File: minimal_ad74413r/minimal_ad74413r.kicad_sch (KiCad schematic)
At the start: 60 parts, among them J1 FW-02-03-G-D-085-155, J2 FW-02-03-G-D-085-155, J3 FW-02-03-G-D-085-155, J4 FW-02-03-G-D-085-155, J5 FW-02-03-G-D-085-155, J6 FW-02-03-G-D-085-155, J7 FW-14-03-G-D-085-155, U1 AD74413RBCPZ

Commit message: Development backup
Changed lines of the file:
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@@
 		(fields_autoplaced yes)
 		(property "Reference" "J4"
-			(at 171.45 30.4799 90)
+			(at 161.29 30.4799 90)
 			(effects
 				(font
 					(size 1.27 1.27)
 				)
-				(justify left)
+				(justify right)
 			)
 		)
 		(property "Value" "FW-02-03-G-D-085-155"
-			(at 171.45 33.0199 90)
+			(at 161.29 33.0199 90)
 			(effects
 				(font
 					(size 1.27 1.27)
 				)
-				(justify left)
+				(justify right)
 			)
 		)

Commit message: Development backup
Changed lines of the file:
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@@
 		(dnp no)
 		(fields_autoplaced yes)
-		(property "Reference" "#PWR7"
+		(property "Reference" "#PWR11"
 			(at 233.68 68.58 0)
 			(effects
@@
 			(project "minimal_ad74413r"
 				(path "/3d1a8eae-9f4e-4ae3-8a80-a6e3408e9f8d"
-					(reference "#PWR7")
+					(reference "#PWR11")
 					(unit 1)
 				)
@@
 		(dnp no)
 		(fields_autoplaced yes)
-		(property "Reference" "#PWR22"
+		(property "Reference" "#PWR3"
 			(at 162.56 74.93 0)
 			(effects
@@
 			(project "minimal_ad74413r"
 				(path "/3d1a8eae-9f4e-4ae3-8a80-a6e3408e9f8d"
-					(reference "#PWR22")
+					(reference "#PWR3")
 					(unit 1)
 				)
@@
 		(dnp no)
 		(fields_autoplaced yes)
-		(property "Reference" "#PWR29"
+		(property "Reference" "#PWR2"
 			(at 137.16 187.96 0)
 			(effects
@@
 			(project "minimal_ad74413r"
 				(path "/3d1a8eae-9f4e-4ae3-8a80-a6e3408e9f8d"
-					(reference "#PWR29")
+					(reference "#PWR2")
 					(unit 1)
 				)
@@
 		(dnp no)
 		(fields_autoplaced yes)
-		(property "Reference" "#PWR6"
+		(property "Reference" "#PWR10"
 			(at 228.6 52.07 0)
 			(effects
@@
 			(project "minimal_ad74413r"
 				(path "/3d1a8eae-9f4e-4ae3-8a80-a6e3408e9f8d"
-					(reference "#PWR6")
+					(reference "#PWR10")
 					(unit 1)
 				)
@@
 		(dnp no)
 		(fields_autoplaced yes)
-		(property "Reference" "#PWR32"
+		(property "Reference" "#PWR15"
 			(at 284.48 137.16 0)
 			(effects
@@
 			(project "minimal_ad74413r"
 				(path "/3d1a8eae-9f4e-4ae3-8a80-a6e3408e9f8d"
-					(reference "#PWR32")
+					(reference "#PWR15")
 					(unit 1)
 				)
@@
 		(dnp no)
 		(fields_autoplaced yes)
-		(property "Reference" "#PWR9"
+		(property "Reference" "#PWR14"
 			(at 243.84 104.14 0)
 			(effects
@@
 			(project "minimal_ad74413r"
 				(path "/3d1a8eae-9f4e-4ae3-8a80-a6e3408e9f8d"
-					(reference "#PWR9")
+					(reference "#PWR14")
 					(unit 1)
 				)
@@
 		(dnp no)
 		(fields_autoplaced yes)
-		(property "Reference" "#PWR36"
+		(property "Reference" "#PWR18"
 			(at 284.48 220.98 0)
 			(effects
@@
 			(project "minimal_ad74413r"
 				(path "/3d1a8eae-9f4e-4ae3-8a80-a6e3408e9f8d"
-					(reference "#PWR36")
+					(reference "#PWR18")
 					(unit 1)
 				)
@@
 		(dnp no)
 		(fields_autoplaced yes)
-		(property "Reference" "#PWR33"
+		(property "Reference" "#PWR16"
 			(at 284.48 165.1 0)
 			(effects
@@
 			(project "minimal_ad74413r"
 				(path "/3d1a8eae-9f4e-4ae3-8a80-a6e3408e9f8d"
-					(reference "#PWR33")
+					(reference "#PWR16")
 					(unit 1)
 				)
@@
 		(dnp no)
 		(fields_autoplaced yes)
-		(property "Reference" "#PWR30"
+		(property "Reference" "#PWR1"
 			(at 121.92 187.96 0)
 			(effects
@@
 			(project "minimal_ad74413r"
 				(path "/3d1a8eae-9f4e-4ae3-8a80-a6e3408e9f8d"
-					(reference "#PWR30")
+					(reference "#PWR1")
 					(unit 1)
 				)
@@
 		(dnp no)
 		(fields_autoplaced yes)
-		(property "Reference" "#PWR4"
+		(property "Reference" "#PWR8"
 			(at 175.26 52.07 0)
 			(effects
@@
 			(project "minimal_ad74413r"
 				(path "/3d1a8eae-9f4e-4ae3-8a80-a6e3408e9f8d"
-					(reference "#PWR4")
+					(reference "#PWR8")
 					(unit 1)
 				)
@@
 		(dnp no)
 		(fields_autoplaced yes)
-		(property "Reference" "#PWR2"
+		(property "Reference" "#PWR7"
 			(at 170.18 219.71 0)
 			(effects
@@
 			(project "minimal_ad74413r"
 				(path "/3d1a8eae-9f4e-4ae3-8a80-a6e3408e9f8d"
-					(reference "#PWR2")
+					(reference "#PWR7")
 					(unit 1)
 				)
@@
 		(dnp no)
 		(fields_autoplaced yes)
-		(property "Reference" "#PWR3"
+		(property "Reference" "#PWR6"
 			(at 167.64 109.22 0)
 			(effects
@@
 			(project "minimal_ad74413r"
 				(path "/3d1a8eae-9f4e-4ae3-8a80-a6e3408e9f8d"
-					(reference "#PWR3")
+					(reference "#PWR6")
 					(unit 1)
 				)
@@
 		(dnp no)
 		(fields_autoplaced yes)
-		(property "Reference" "#PWR8"
+		(property "Reference" "#PWR12"
 			(at 238.76 86.36 0)
 			(effects
@@
 			(project "minimal_ad74413r"
 				(path "/3d1a8eae-9f4e-4ae3-8a80-a6e3408e9f8d"
-					(reference "#PWR8")
+					(reference "#PWR12")
 					(unit 1)
 				)
@@
 		(dnp no)
 		(fields_autoplaced yes)
-		(property "Reference" "#PWR1"
+		(property "Reference" "#PWR4"
 			(at 162.56 87.63 0)
 			(effects
@@
 			(project "minimal_ad74413r"
 				(path "/3d1a8eae-9f4e-4ae3-8a80-a6e3408e9f8d"
-					(reference "#PWR1")
+					(reference "#PWR4")
 					(unit 1)
 				)
@@
 		(on_board yes)
 		(dnp no)
-		(property "Reference" "#PWR28"
+		(property "Reference" "#PWR5"
 			(at 167.64 45.72 0)
 			(effects
@@
 			(project "minimal_ad74413r"
 				(path "/3d1a8eae-9f4e-4ae3-8a80-a6e3408e9f8d"
-					(reference "#PWR28")
+					(reference "#PWR5")
 					(unit 1)
 				)
@@
 		(dnp no)
 		(fields_autoplaced yes)
-		(property "Reference" "#PWR5"
+		(property "Reference" "#PWR9"
 			(at 203.2 243.84 0)
 			(effects
@@
 			(project "minimal_ad74413r"
 				(path "/3d1a8eae-9f4e-4ae3-8a80-a6e3408e9f8d"
-					(reference "#PWR5")
+					(reference "#PWR9")
 					(unit 1)
 				)
@@
 		(dnp no)
 		(fields_autoplaced yes)
-		(property "Reference" "#PWR34"
+		(property "Reference" "#PWR17"
 			(at 284.48 193.04 0)
 			(effects
@@
 			(project "minimal_ad74413r"
 				(path "/3d1a8eae-9f4e-4ae3-8a80-a6e3408e9f8d"
-					(reference "#PWR34")
+					(reference "#PWR17")
 					(unit 1)
 				)
@@
 		(on_board yes)
 		(dnp no)
-		(property "Reference" "#PWR27"
+		(property "Reference" "#PWR13"
 			(at 241.3 45.72 0)
 			(effects
@@
 			(project "minimal_ad74413r"
 				(path "/3d1a8eae-9f4e-4ae3-8a80-a6e3408e9f8d"
-					(reference "#PWR27")
+					(reference "#PWR13")
 					(unit 1)
 				)

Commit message: Development backup
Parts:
- removed J3, J4: FW-02-03-G-D-085-155, connector_footprints:FW-02-03-G-D-085-155, symbol UNITED_CONNECTORS_DATA_BASE:J_FW-02-03-G-D-085-155
- removed MB3, MB4: mouse-bite-midle-50mil-200mil, mouse_bite_footprints:mouse-bite-midle-50mil-200mil, symbol UNITED_MOUSE_BITES_DATA_BASE:mouse-bite-midle-50mil-200mil
- removed TP25, TP26: TestPoint, test_point_footprints:TestPoint_THTPad_Castelated, symbol UNITED_TEST_POINTS:TestPoint_Castelated
- added C33: 4.7 µF, capacitor_footprints:C_1210_200_3225Metric, symbol UNITED_CAPACITORS_DATA_BASE:C_GCM32DC72A475KE02K
- added C34, C35, C36, C41, C43: 100 nF, capacitor_footprints:C_0402_1005Metric, symbol UNITED_CAPACITORS_DATA_BASE:C_GCM155R71H104KE02D
- added C37, C38: 10 µF, capacitor_footprints:C_1206_3216Metric, symbol UNITED_CAPACITORS_DATA_BASE:C_CL31B106KBHNNN#
- added C39: 4.7 µF, capacitor_footprints:C_0603_1608Metric, symbol UNITED_CAPACITORS_DATA_BASE:C_C1608X7S1A475K080AC
- added C40, C42: 1 nF, capacitor_footprints:C_0402_1005Metric, symbol UNITED_CAPACITORS_DATA_BASE:C_GCM155R71H102KA37D
- added D5: 62.0 V, diode_footprints:SOD_123, symbol UNITED_DIODES_DATA_BASE:D_MMSZ5265BT1G
- added D6: 100.0 V, diode_footprints:PowerDI_123, symbol UNITED_DIODES_DATA_BASE:D_DFLS1200-7
- added D7: 200.0 V, diode_footprints:SOD_123F, symbol UNITED_DIODES_DATA_BASE:D_US1DWF
- added J8: FW-02-03-G-D-085-155, connector_footprints:FW-02-03-G-D-085-155, symbol UNITED_CONNECTORS_DATA_BASE:J_FW-02-03-G-D-085-155
- added JP1: SolderJumper_3_Open, solder_jumper_footprints:SolderJumper-3_P1.3mm_Open_RoundedPad1.0x1.5mm_NumberLabels, symbol UNITED_SOLDER_JUMPERS:SolderJumper_3_Open
- added JP2, JP3: SolderJumper_2_Bridged, solder_jumper_footprints:SolderJumper-2_P1.3mm_Bridged_RoundedPad1.0x1.5mm, symbol UNITED_SOLDER_JUMPERS:SolderJumper_2_Bridged
- added L1: 100 µH, inductor_footprints:XFL3012, symbol UNITED_INDUCTORS_DATA_BASE:L_XFL3012-104ME
- added R21, R22, R23, R24, R25, R26, R27, R28: 100 kΩ, resistor_footprints:R_0402_1005Metric, symbol UNITED_RESISTORS_DATA_BASE:R_ERJ-2GEJ104X
- added T1: ZA9644-AED, transformer_footprints:ZA9644, symbol UNITED_TRANSFORMERS_DATA_BASE:T_ZA9644-AED
- added U2: ADP1032ACPZ-5-R7, analog_devices_footprints:CP-41-1_ADI, symbol UNITED_IC_ADI:U_ADP1032ACPZ-5-R7
- added U3: MAX22440CAEE+, analog_devices_footprints:21-0055_E16MS&plus_1F_ADI, symbol UNITED_IC_ADI:U_MAX22440CAEE+
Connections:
- net 3V3: now also C35.1, C36.1, C42.1, C43.1, JP2.2, R23.1, R25.1, R27.1, U2.10 (SVDD1), U2.20 (SVDD2), U3.1 (VDDA); no longer J7.13, TP19.1
- net GNDA: now also C35.2, C36.2, C37.2, C38.2, C39.2, C42.2, C43.2, R22.1, R24.2, R26.2, R28.2, T1.8, U2.16 (SGND2), U2.27 (SGND2), U2.4 (SGND2), U2.44 (EPGND2), U2.5 (SGND1), U3.2 (GNDA), U3.8 (GNDA); no longer J7.10, J7.11, J7.12, J7.14, J7.16, J7.18, J7.2, J7.20, J7.22, J7.24, J7.26, J7.28, J7.4, J7.6, J7.8, TP18.1, TP5.1, TP6.1
- net GPO_A: now also J7.23, TP8.1, U3.14 (OUT1); no longer J7.27, U1.19 (GPO_A)
- net GPO_B: now also J7.21, TP7.1, U3.13 (OUT2); no longer J7.25, U1.20 (GPO_B)
- net GPO_C: now also J7.19, TP14.1, U3.12 (OUT3); no longer J7.1, TP13.1, U1.21 (GPO_C)
- net GPO_D: now also J7.17, TP13.1, U3.11 (OUT4); no longer J7.3, TP14.1, U1.22 (GPO_D)
- net SCLK: now also R23.2, U2.9 (SCK); no longer J7.17, TP21.1
- net SDI: now also R28.1, U2.8 (SI); no longer J7.19, TP22.1
- net SDO: now also R24.1, U2.7 (SO); no longer J7.5, TP15.1
- net VDD_24V: now also JP3.2; no longer TP7.1, TP8.1
- net ~{ADC_RDY}: now also J7.15, TP17.1; no longer J7.7, TP16.1
- net ~{ALERT}: now also R27.2, U2.21 (SGPI3); no longer J7.9, TP17.1
- net ~{LDAC}: now also R26.1, U2.22 (SGPO2); no longer J7.15, TP20.1
- net ~{RESET}: now also R25.2, U2.23 (SGPO1); no longer J7.23, TP24.1
- net ~{SYNC}: now also U2.6 (~{SSS}); no longer J7.21, TP23.1
- new net: D5.1, D6.1
- new net: R22.2, U2.14 (SYNC)
- new net: R21.2, U2.35 (PWRGD)
- new net: D7.2, T1.5
- new net GND: C33.1, J8.1, J8.2, JP1.3 (B), TP16.1, U2.28 (PGNDP), U2.33 (GNDP), U2.43 (EPGNDP)
- new net GNDD: C34.2, C40.2, C41.2, J7.10, J7.12, J7.14, J7.16, J7.18, J7.2, J7.20, J7.22, J7.24, J7.25, J7.26, J7.4, J7.6, J7.8, TP6.1, U2.3 (MGND), U2.34 (MGND), U2.42 (EPGNDM), U3.15 (GNDB), U3.9 (GNDB)
- new net GPO_A_ISO: U1.19 (GPO_A), U3.3 (IN1)
- new net GPO_B_ISO: U1.20 (GPO_B), U3.4 (IN2)
- new net GPO_C_ISO: U1.21 (GPO_C), U3.5 (IN3)
- new net GPO_D_ISO: U1.22 (GPO_D), U3.6 (IN4)
- new net MCK: J7.7, TP21.1, U2.40 (MCK)
- new net MGPI1: J7.1, TP24.1, U2.36 (MGPI1)
- new net MGPI2: J7.3, TP23.1, U2.37 (MGPI2)
- new net MGPO3: J7.5, TP22.1, U2.38 (MGPO3)
- new net MI: J7.11, TP19.1, U2.1 (MI)
- new net MO: J7.9, TP20.1, U2.41 (MO)
- new net MVDD: C34.1, C40.1, C41.1, J7.27, J7.28, R21.1, TP5.1, U2.39 (MVDD), U3.10 (ENB), U3.16 (VDDB)
- new net SLEW: JP1.2 (C), U2.32 (SLEW)
- new net SW2: L1.1, U2.17 (SW2)
- new net SWP: D6.2, T1.4, U2.29 (SWP)
- new net VINP: C33.2, D5.2, J8.3, J8.4, JP1.1 (A), T1.1, TP15.1, U2.30 (VINP), U2.31 (EN)
- new net VOUT1: C37.1, C38.1, D7.1, JP3.1, U2.18 (VOUT1)
- new net VOUT2: C39.1, JP2.1, L1.2, U2.15 (VOUT2)
- new net ~{MSS}: J7.13, TP18.1, U2.2 (~{MSS})
- no-connect marks 1 -> 2
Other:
- moved on the sheet: C1, C14, C15, C16, C17, C18, C19, C2, C20, C29, C3, C30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

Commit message: Development backup
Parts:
- removed C40, C42: 1 nF, capacitor_footprints:C_0402_1005Metric, symbol UNITED_CAPACITORS_DATA_BASE:C_GCM155R71H102KA37D
- removed C41, C43: 100 nF, capacitor_footprints:C_0402_1005Metric, symbol UNITED_CAPACITORS_DATA_BASE:C_GCM155R71H104KE02D
- removed U3: MAX22440CAEE+, analog_devices_footprints:21-0055_E16MS&plus_1F_ADI, symbol UNITED_IC_ADI:U_MAX22440CAEE+
- added C44, C45: 100 nF, capacitor_footprints:C_0402_1005Metric, symbol UNITED_CAPACITORS_DATA_BASE:C_GCM155R71H104KE02D
- added J9: FW-02-03-G-D-085-155, connector_footprints:FW-02-03-G-D-085-155, symbol UNITED_CONNECTORS_DATA_BASE:J_FW-02-03-G-D-085-155
- added MB8, MB9: mouse-bite-midle-50mil-200mil, mouse_bite_footprints:mouse-bite-midle-50mil-200mil, symbol UNITED_MOUSE_BITES_DATA_BASE:mouse-bite-midle-50mil-200mil
- added TP25, TP26: TestPoint, test_point_footprints:TestPoint_THTPad_Castelated, symbol UNITED_TEST_POINTS:TestPoint_Castelated
- added U4: MAX22166EAEE+T, analog_devices_footprints:21-0055_E16MS&plus_2_MXM_ADI, symbol UNITED_IC_ADI:U_MAX22166EAEE+T
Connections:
- net 3V3: now also C44.1, U4.1 (VDDA)
- net GND: now also J8.3; no longer J8.2
- net GNDA: now also C44.2, J9.1, J9.3, TP26.1, U4.8 (GNDA)
- net GNDD: now also J7.17, J7.28, TP13.1, C45.2, U4.9 (GNDB); no longer J7.16, J7.25, TP6.1
- net GPO_A: now also J7.27, TP5.1, U4.14 (OUT2); no longer J7.23, TP8.1
- net GPO_A_ISO: now also U4.3 (IN2)
- net GPO_B: now also J7.25, TP6.1, U4.13 (OUT3); no longer J7.21, TP7.1
- net GPO_B_ISO: now also U4.4 (IN3)
- net GPO_C: now also J7.23, TP8.1, U4.12 (OUT4); no longer J7.19, TP14.1
- net GPO_C_ISO: now also U4.5 (IN4)
- net GPO_D: now also J7.21, TP7.1, U4.11 (OUT5); no longer J7.17, TP13.1
- net GPO_D_ISO: now also U4.6 (IN5)
- net MVDD: now also J7.15, J7.16, TP17.1, C45.1, U4.16 (VDDB); no longer J7.27, J7.28, TP5.1
- net VDD_24V: now also J9.2, J9.4, TP25.1
- net VINP: now also J8.2; no longer J8.3
- net ~{ADC_RDY}: now also J7.19, TP14.1, U4.10 (OUT6); no longer J7.15, TP17.1, U1.52 (~{ADC_RDY})
- new net ~{ADC_RDY_ISO}: U1.52 (~{ADC_RDY}), U4.7 (IN6)
- no-connect marks 2 -> 4
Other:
- moved on the sheet: J8, TP15, TP16

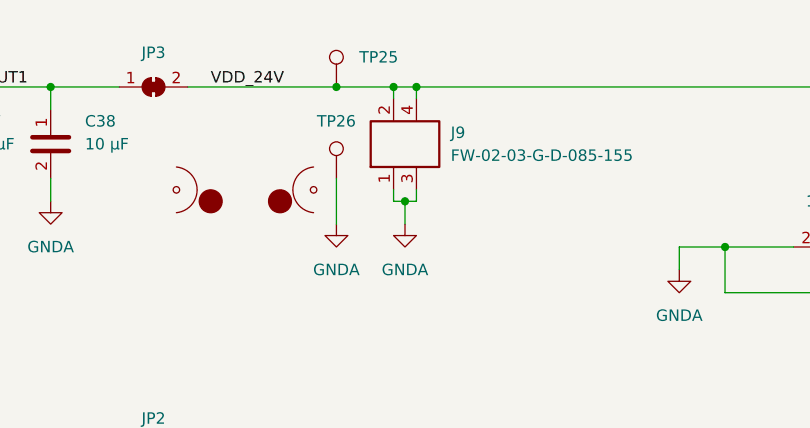
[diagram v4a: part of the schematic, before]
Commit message: update minimal_ad74413r footprint
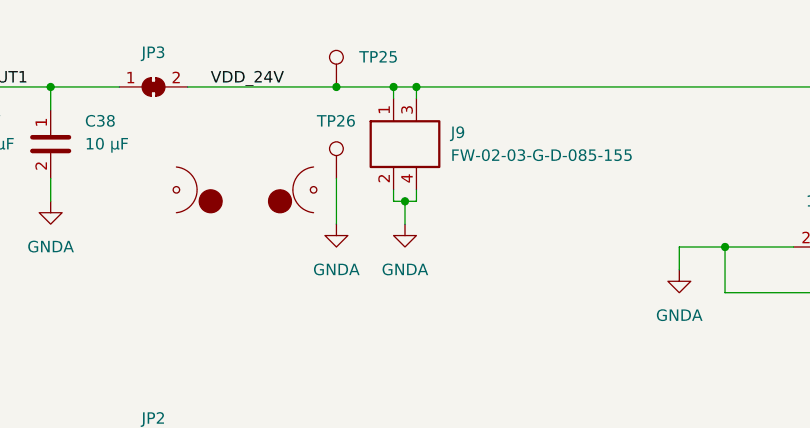
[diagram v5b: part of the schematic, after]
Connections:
- net GNDA: now also J9.2, J9.4; no longer J9.1, J9.3
- net VDD_24V: now also J9.1, J9.3; no longer J9.2, J9.4
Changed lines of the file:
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@@
 		(lib_id "UNITED_CONNECTORS_DATA_BASE:J_FW-02-03-G-D-085-155")
 		(at 215.9 34.29 90)
+		(mirror x)
 		(unit 1)
 		(exclude_from_sim no)
@@
 		)
 		(property "Footprint" "connector_footprints:FW-02-03-G-D-085-155"
-			(at 223.52 29.21 0)
+			(at 223.52 39.37 0)
 			(show_name yes)
 			(effects
@@
 		)
 		(property "Datasheet" "https://suddendocs.samtec.com/catalog_english/fw_sm.pdf?_gl=1*1xtxv9c*_gcl_au*MTM0MTYyNTQ5MS4xNzM2MDk5MTUz*_ga*MTYxNDYyMTQ0Mi4xNzM2MDk5MTUz*_ga_3KFNZC07WW*MTczODE2NTI0NS4zMi4xLjE3MzgxNjU1NjMuNjAuMC4w"
-			(at 226.06 29.21 0)
+			(at 226.06 39.37 0)
 			(show_name yes)
 			(effects
@@
 		)
 		(property "Description" "Samtec FW-xx-03-G-D-085-155 series,  2 positions connector,  1.27 mm pitch,  Black,  Vertical mounting,  5.2 A,  300 V,  Surface Mount,  Gold plated"
-			(at 228.6 29.21 0)
+			(at 228.6 39.37 0)
 			(show_name yes)
 			(effects
@@
 		)
 		(property "Color" "Black"
-			(at 231.14 29.21 0)
+			(at 231.14 39.37 0)
 			(show_name yes)
 			(effects
@@
 		)
 		(property "Contact Plating" "Gold"
-			(at 233.68 29.21 0)
+			(at 233.68 39.37 0)
 			(show_name yes)
 			(effects
@@
 		)
 		(property "Current Rating (A)" "5.2"
-			(at 236.22 29.21 0)
+			(at 236.22 39.37 0)
 			(show_name yes)
 			(effects
@@
 		)
 		(property "MPN" "FW-02-03-G-D-085-155"
-			(at 238.76 29.21 0)
+			(at 238.76 39.37 0)
 			(show_name yes)
 			(effects
@@
 		)
 		(property "Manufacturer" "Samtec"
-			(at 241.3 29.21 0)
+			(at 241.3 39.37 0)
 			(show_name yes)
 			(effects
@@
 		)
 		(property "Mounting Angle" "Vertical"
-			(at 243.84 29.21 0)
+			(at 243.84 39.37 0)
 			(show_name yes)
 			(effects
@@
 		)
 		(property "Mounting Style" "Surface Mount"
-			(at 246.38 29.21 0)
+			(at 246.38 39.37 0)
 			(show_name yes)
 			(effects
@@
 		)
 		(property "Number of Rows" "2"
-			(at 248.92 29.21 0)
+			(at 248.92 39.37 0)
 			(show_name yes)
 			(effects
@@
 		)
 		(property "Pin Count" "2"
-			(at 251.46 29.21 0)
+			(at 251.46 39.37 0)
 			(show_name yes)
 			(effects
@@
 		)
 		(property "Pitch (mm)" "1.27"
-			(at 254 29.21 0)
+			(at 254 39.37 0)
 			(show_name yes)
 			(effects
@@
 		)
 		(property "Series" "FW-xx-03-G-D-085-155"
-			(at 256.54 29.21 0)
+			(at 256.54 39.37 0)
 			(show_name yes)
 			(effects
@@
 		)
 		(property "Symbol Name" "J_FW-02-03-G-D-085-155"
-			(at 259.08 29.21 0)
+			(at 259.08 39.37 0)
 			(show_name yes)
 			(effects
@@
 		)
 		(property "Trustedparts Search" "https://www.trustedparts.com/en/search/FW-02-03-G-D-085-155"
-			(at 261.62 29.21 0)
+			(at 261.62 39.37 0)
 			(show_name yes)
 			(effects
@@
 		)
 		(property "Voltage Rating (V)" "300"
-			(at 264.16 29.21 0)
-			(show_name yes)
-			(effects
+			(at 264.16 39.37 0)
+			(show_name yes)
+			(effects

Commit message: Development backup
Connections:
- net GPO_A: now also J7.21, TP7.1, U4.11 (OUT5); no longer J7.27, TP5.1, U4.14 (OUT2)
- net GPO_A_ISO: now also U4.6 (IN5); no longer U4.3 (IN2)
- net GPO_B: now also J7.23, TP8.1, U4.12 (OUT4); no longer J7.25, TP6.1, U4.13 (OUT3)
- net GPO_B_ISO: now also U4.5 (IN4); no longer U4.4 (IN3)
- net GPO_C: now also J7.25, TP6.1, U4.13 (OUT3); no longer J7.23, TP8.1, U4.12 (OUT4)
- net GPO_C_ISO: now also U4.4 (IN3); no longer U4.5 (IN4)
- net GPO_D: now also J7.27, TP5.1, U4.14 (OUT2); no longer J7.21, TP7.1, U4.11 (OUT5)
- net GPO_D_ISO: now also U4.3 (IN2); no longer U4.6 (IN5)
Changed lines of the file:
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@@
 	)
 	(label "GPO_B"
-		(at 72.39 264.16 0)
+		(at 72.39 261.62 0)
 		(effects
 			(font
@@
 	)
 	(label "GPO_C"
-		(at 72.39 261.62 0)
+		(at 72.39 264.16 0)
 		(effects
 			(font
@@
 	)
 	(label "GPO_B_ISO"
-		(at 153.67 176.53 180)
+		(at 153.67 179.07 180)
 		(effects
 			(font
@@
 	)
 	(label "GPO_A"
-		(at 72.39 266.7 0)
+		(at 72.39 259.08 0)
 		(effects
 			(font
@@
 	)
 	(label "GPO_D"
-		(at 105.41 181.61 0)
+		(at 105.41 173.99 0)
 		(effects
 			(font
@@
 	)
 	(label "GPO_B"
-		(at 105.41 176.53 0)
+		(at 105.41 179.07 0)
 		(effects
 			(font
@@
 	)
 	(label "GPO_D_ISO"
-		(at 153.67 181.61 180)
+		(at 153.67 173.99 180)
 		(effects
 			(font
@@
 	)
 	(label "GPO_C"
-		(at 105.41 179.07 0)
+		(at 105.41 176.53 0)
 		(effects
 			(font
@@
 	)
 	(label "GPO_A"
-		(at 105.41 173.99 0)
+		(at 105.41 181.61 0)
 		(effects
 			(font
@@
 	)
 	(label "GPO_C_ISO"
-		(at 153.67 179.07 180)
+		(at 153.67 176.53 180)
 		(effects
 			(font
@@
 	)
 	(label "GPO_D"
-		(at 72.39 259.08 0)
+		(at 72.39 266.7 0)
 		(effects
 			(font
@@
 	)
 	(label "GPO_A_ISO"
-		(at 153.67 173.99 180)
-		(effects
-			(font
+		(at 153.67 181.61 180)
+		(effects
+			(font
